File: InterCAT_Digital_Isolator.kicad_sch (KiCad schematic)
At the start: 24 parts, among them U10 MAX3250, U11 EL357N(C)(TA)-G, U12 EL357N(C)(TA)-G, U8 EL357N(C)(TA)-G, U9 EL357N(C)(TA)-G

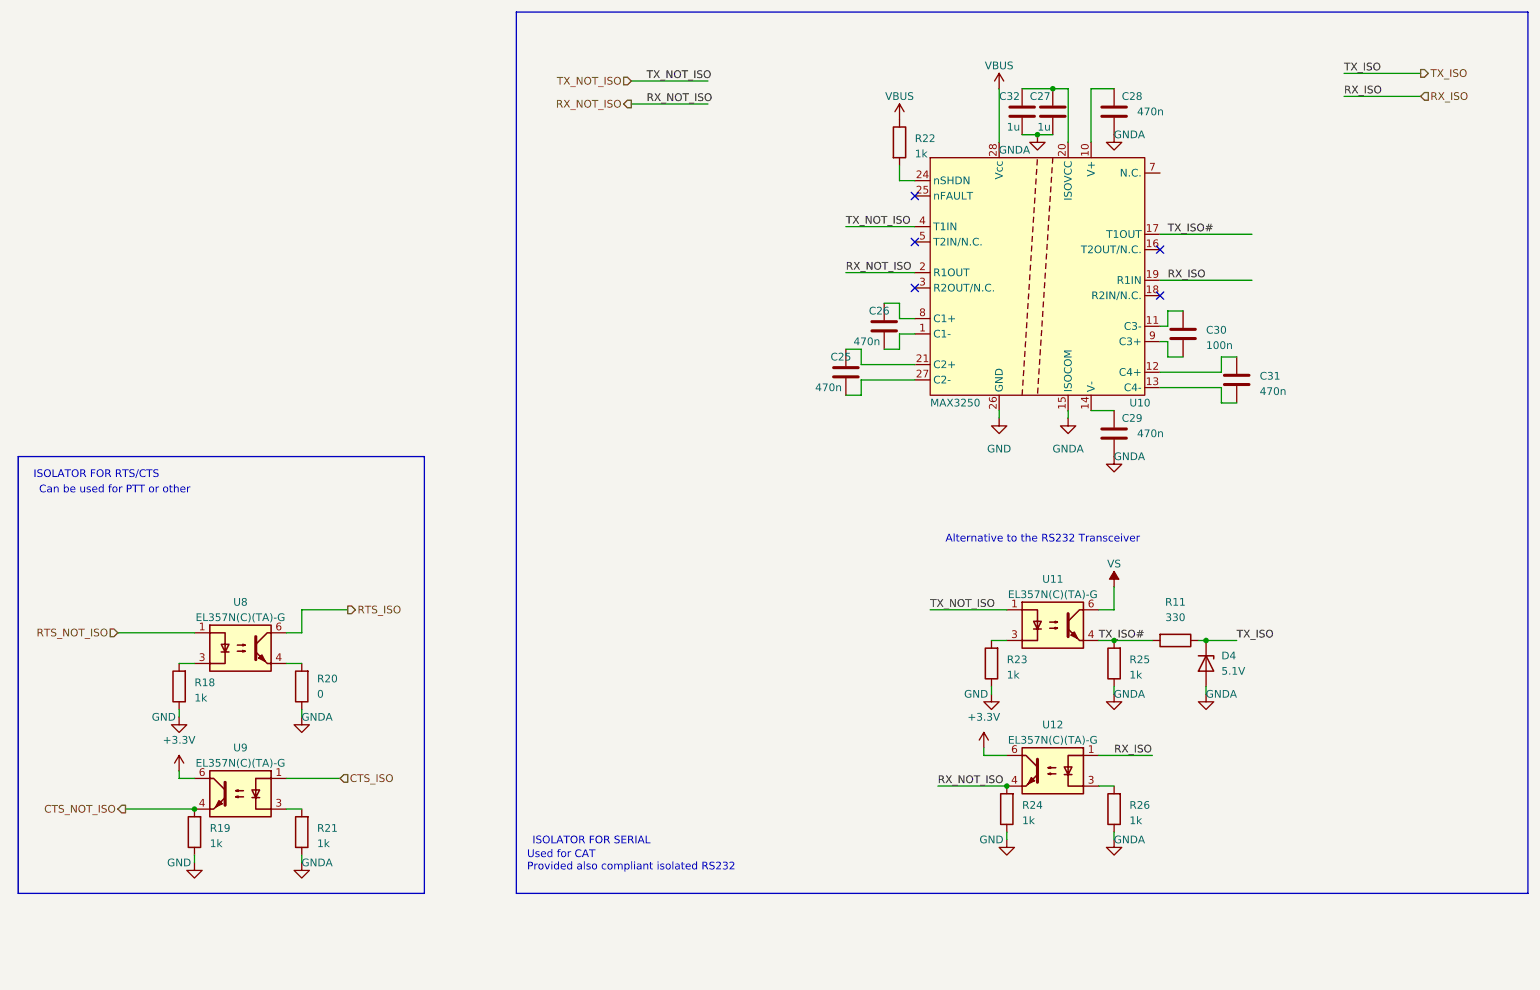
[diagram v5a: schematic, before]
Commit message: added iso bypass, removed RS232, added Extra opto and prog connector
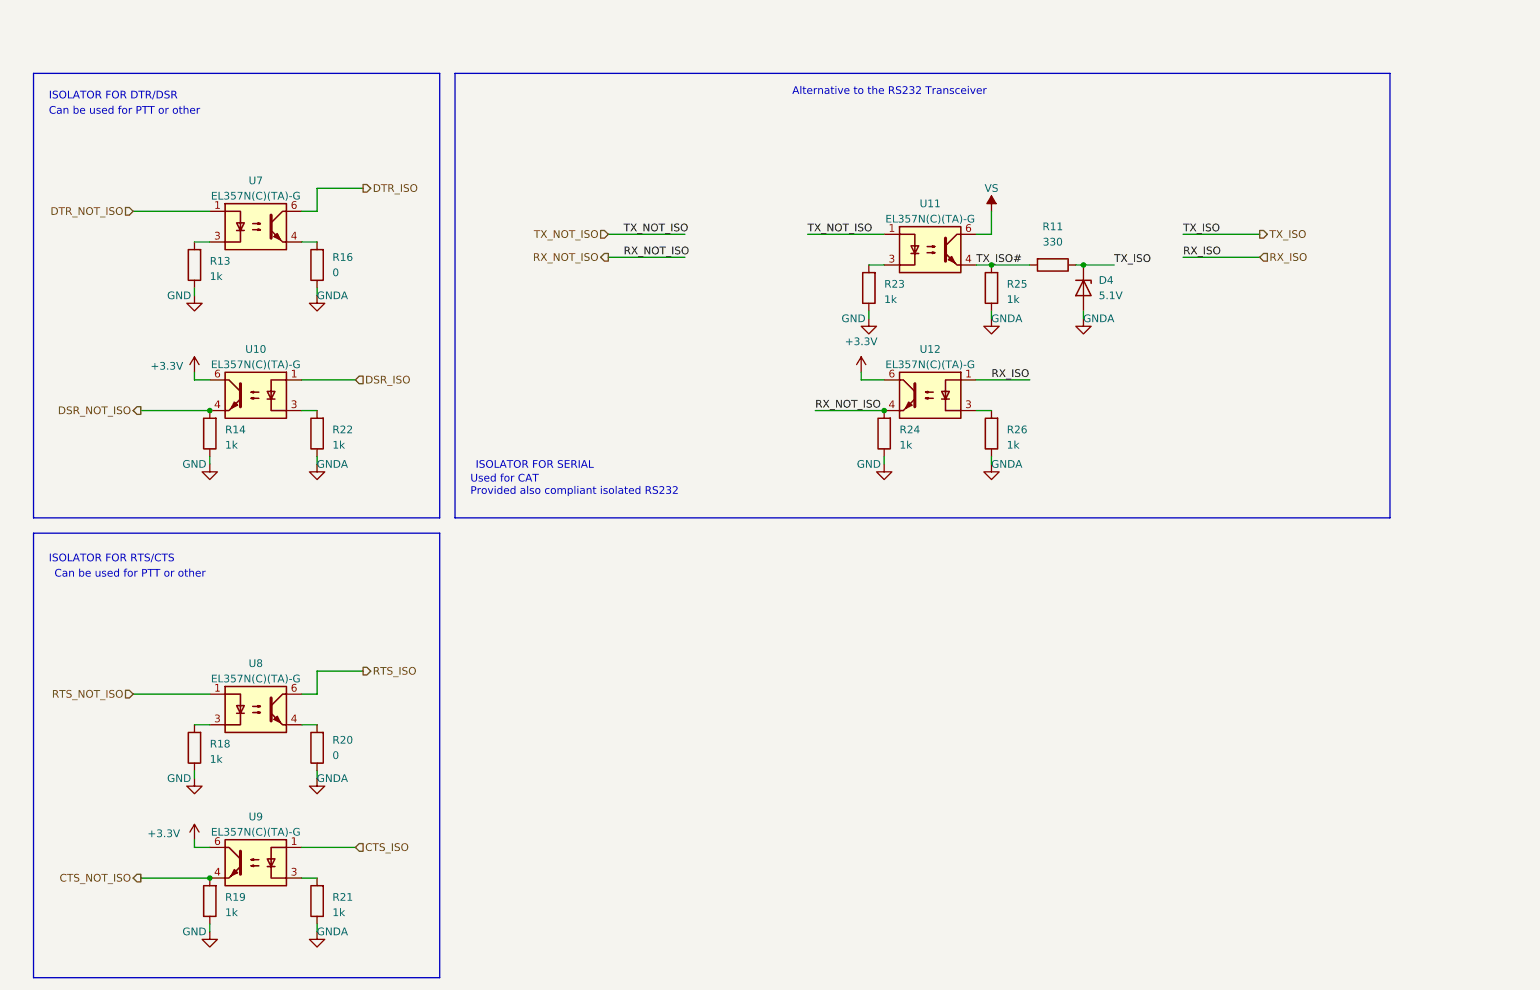
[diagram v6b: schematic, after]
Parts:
- removed C25, C26, C28, C29, C31: 470n, Capacitor_SMD:C_0603_1608Metric, symbol Device:C
- removed C27, C32: 1u, Capacitor_SMD:C_0805_2012Metric, symbol Device:C
- removed C30: 100n, Capacitor_SMD:C_0603_1608Metric, symbol Device:C
- removed U10: MAX3250, Package_SO:SSOP-28_5.3x10.2mm_P0.65mm, symbol InterCat:MAX3250
- added R13, R14: 1k, Resistor_SMD:R_0603_1608Metric, symbol Device:R
- added R16: 0, Resistor_SMD:R_0603_1608Metric, symbol Device:R
- added U10, U7: EL357N(C)(TA)-G, InterCat:SO-6-4_4.4x3.9mm_P2.54mm, symbol Isolator:TLP185
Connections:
- net VBUS is gone; now on net GNDA: R22.1
- net +3.3V: now also U10.6
- net GND: now also R13.1, R14.1
- net GNDA: now also R16.1
- net at R22.2: now also U10.3
- new net: R13.2, U7.3
- new net: R16.2, U7.4
- new net DSR_ISO: U10.1
- new net DSR_NOT_ISO: R14.2, U10.4
- new net DTR_ISO: U7.6
- new net DTR_NOT_ISO: U7.1
- no-connect marks 5 -> 0
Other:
- note added: "ISOLATOR FOR DTR/DSR"
- moved on the sheet: D4, R11, R18, R19, R20, R21, R23, R24, R25, R26, U11, U12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
